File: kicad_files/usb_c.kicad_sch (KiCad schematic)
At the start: 5 parts, among them J4 USB_C_Receptacle_USB2.0_14P, U3 USBLC6-2SC6

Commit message: Change USB Connector
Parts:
- J4: footprint Connector_USB:USB_C_Receptacle_HRO_TYPE-C-31-M-12 -> Connector_USB:USB_C_Receptacle_G-Switch_GT-USB-7010ASV
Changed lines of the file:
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@@
 			)
 		)
-		(property "Footprint" "Connector_USB:USB_C_Receptacle_HRO_TYPE-C-31-M-12"
+		(property "Footprint" "Connector_USB:USB_C_Receptacle_G-Switch_GT-USB-7010ASV"
 			(at 45.085 50.8 0)
 			(effects

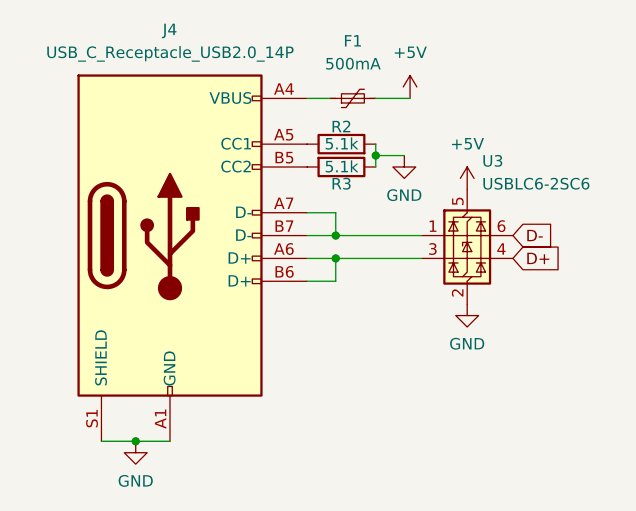
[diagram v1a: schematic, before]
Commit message: rev1.1
1. Changed reset/boot circuitry to have single-button Reset/Boot functionality.
2. Removed mounting holes
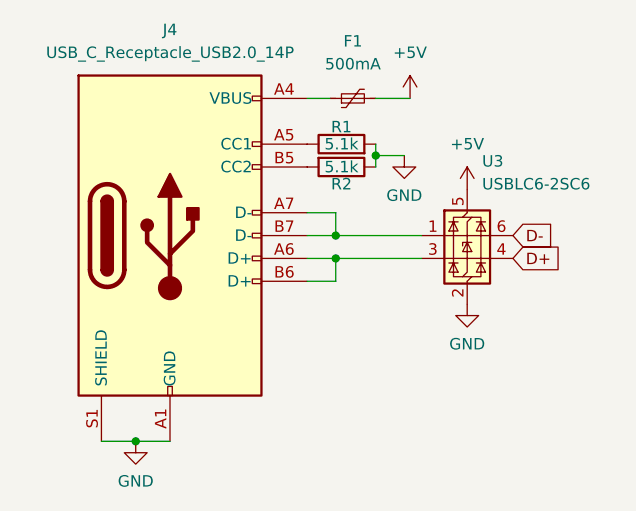
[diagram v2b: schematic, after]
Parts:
- renumbered R2 to R1, R3 to R2
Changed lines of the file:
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@@
 		(on_board yes)
 		(dnp no)
-		(property "Reference" "R2"
+		(property "Reference" "R1"
 			(at 60.325 38.735 90)
 			(effects
@@
 			(project ""
 				(path "/3657237e-c8f2-4ecf-b631-303d8d00a2b6/de27cc8e-3132-4798-a774-94c49c9a441c"
-					(reference "R2")
+					(reference "R1")
 					(unit 1)
 				)
@@
 		(on_board yes)
 		(dnp no)
-		(property "Reference" "R3"
+		(property "Reference" "R2"
 			(at 60.325 45.085 90)
 			(effects
@@
 			(project "bonk"
 				(path "/3657237e-c8f2-4ecf-b631-303d8d00a2b6/de27cc8e-3132-4798-a774-94c49c9a441c"
-					(reference "R3")
-					(unit 1)
-				)
+					(reference "R2")
+					(unit 1)
+				)
